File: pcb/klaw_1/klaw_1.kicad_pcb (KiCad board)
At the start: 2 copper layers, 128.2 x 99 mm, 71 parts, among them J1 PJ-320A-4P, J3 lv27, SW1 SW_PUSH-MX_W_LED, SW10 SW_PUSH-MX_W_LED, SW12 SW_PUSH-MX_W_LED, SW13 SW_PUSH-MX_W_LED, SW14 SW_PUSH-MX_W_LED, SW15 SW_PUSH-MX_W_LED, SW16 SW_PUSH-MX_W_LED, SW18 EC11E15244G1, SW2 SW_PUSH-MX_W_LED, SW20 SW_PUSH-MX_W_LED, SW21 SW_PUSH-MX_W_LED, SW3 SW_PUSH-MX_W_LED, SW4 SW_PUSH-MX_W_LED, SW5 SW_PUSH-MX_W_LED, SW6 SW_PUSH-MX_W_LED, SW7 SW_PUSH-MX_W_LED, SW8 SW_PUSH-MX_W_LED, SW9 SW_PUSH-MX_W_LED, U1 ProMicro

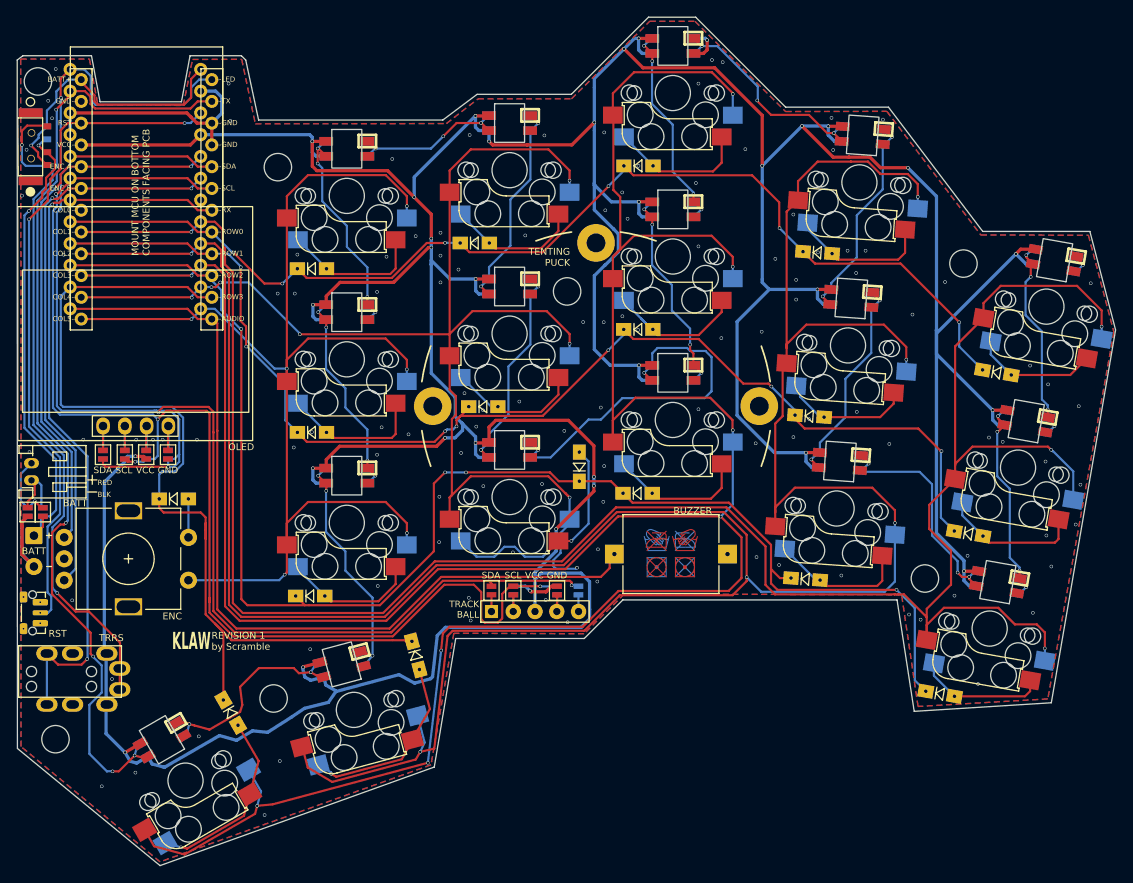
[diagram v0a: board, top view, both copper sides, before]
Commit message: feat: rev 2 - machine-assemblable LEDs (SK6812MINI-EA)
- LED footprint reworked for SK6812MINI-EA: 3.8x3.4 window per
  datasheet, EA land pattern, per-face pin maps chosen to preserve
  LED chain routing (F side rotated 180)
- LED chain start jumper JP26 removed; LED net routed directly
- sourcing swapped to C5378731 with MPN fields; LEDs marked as
  JLC-assembled, sockets remain hand-solder
- fab refresh: rev-2 gerbers, LED placement rows in both CPLs
  (41 placements/side), READMEs updated
- new EA 3D model
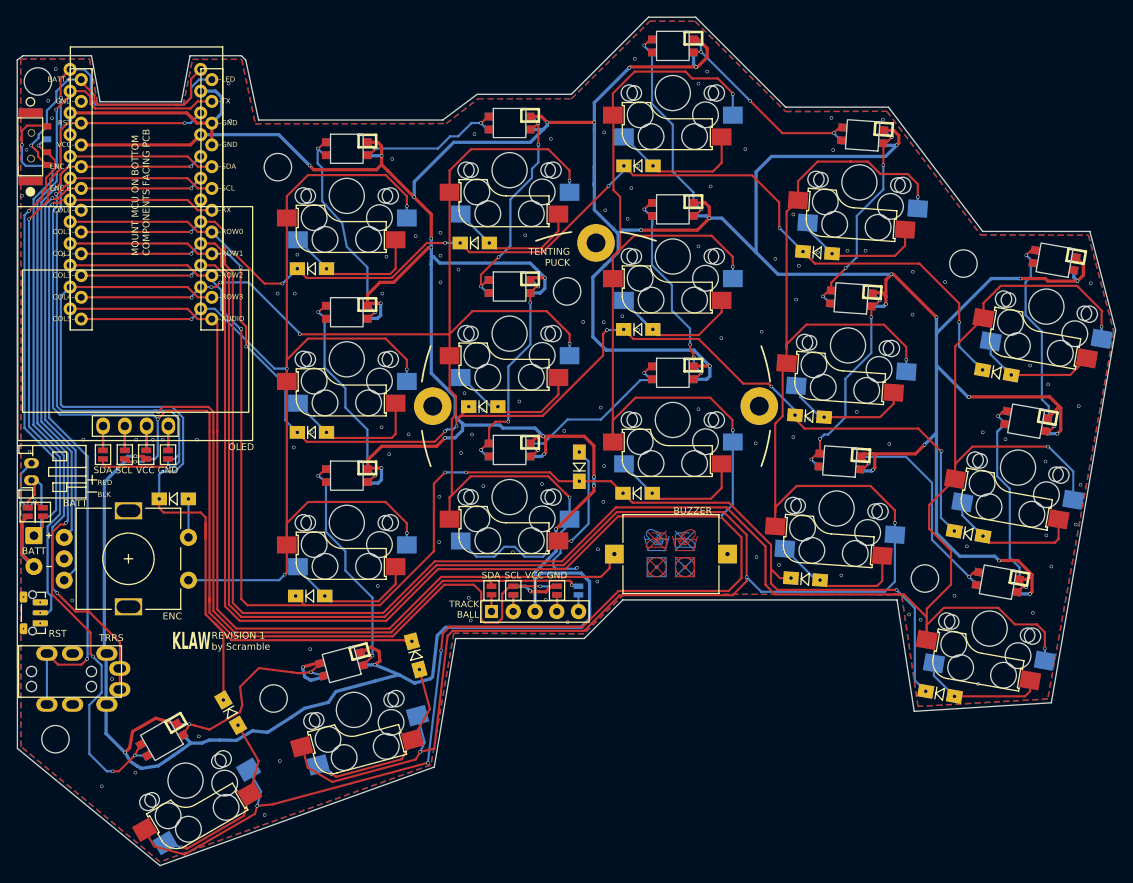
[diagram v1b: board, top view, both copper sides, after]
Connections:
- SW20 pad 3: Net-(SW20B-DIN) -> LED
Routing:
- net Net-(SW13B-DOUT): track 42.3 -> 22.4 mm
- net LED: track 112.3 -> 118.6 mm, vias 3 -> 5
- net Net-(SW20B-DOUT): track 24.1 -> 30.3 mm, vias 2 -> 3
- net Net-(SW20B-DIN): track 5.81 -> 0.00 mm, vias 2 -> 0
- net GND: track 54.0 -> 49.5 mm, vias 121 -> 120
- net VCC: track 600.8 -> 604.3 mm, vias 31 -> 36
- net Net-(SW2B-DOUT): track 24.3 -> 27.1 mm, vias 2 -> 4
- net (no net): track 2.34 -> 0.00 mm, vias 1 -> 0
- net Net-(SW10B-DIN): track 24.0 -> 26.3 mm, vias 4 -> 2
- net Net-(SW13B-DIN): track 24.2 -> 25.7 mm, vias 2 -> 4
- net Net-(SW14B-DOUT): track 24.3 -> 25.6 mm
- net row0: track 130.0 -> 131.3 mm
- net row1: track 143.9 -> 145.1 mm
- net Net-(SW10B-DOUT): track 24.0 -> 25.0 mm, vias 4 -> 2
- net Net-(SW15B-DIN): track 24.3 -> 25.1 mm, vias 2 -> 4
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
